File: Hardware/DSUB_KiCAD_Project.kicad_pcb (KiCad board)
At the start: 4 copper layers, 112.2 x 87.2 mm, 6 parts, among them J1 DB37_Female, J11 DB37_Female, J3 DB37_Female, J5 DB37_Female, J7 DB37_Female, J9 DB37_Female

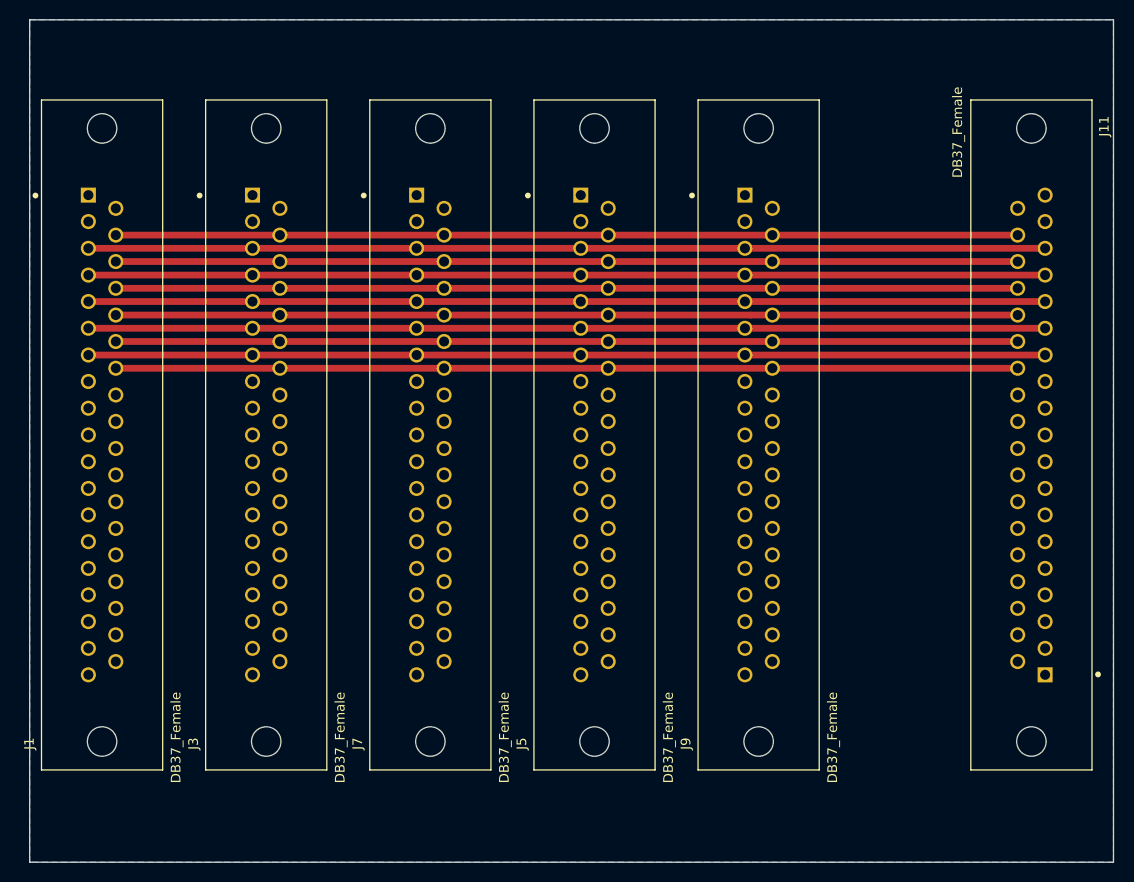
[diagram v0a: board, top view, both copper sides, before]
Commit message: rounded corners
corners were rounded to 5mm
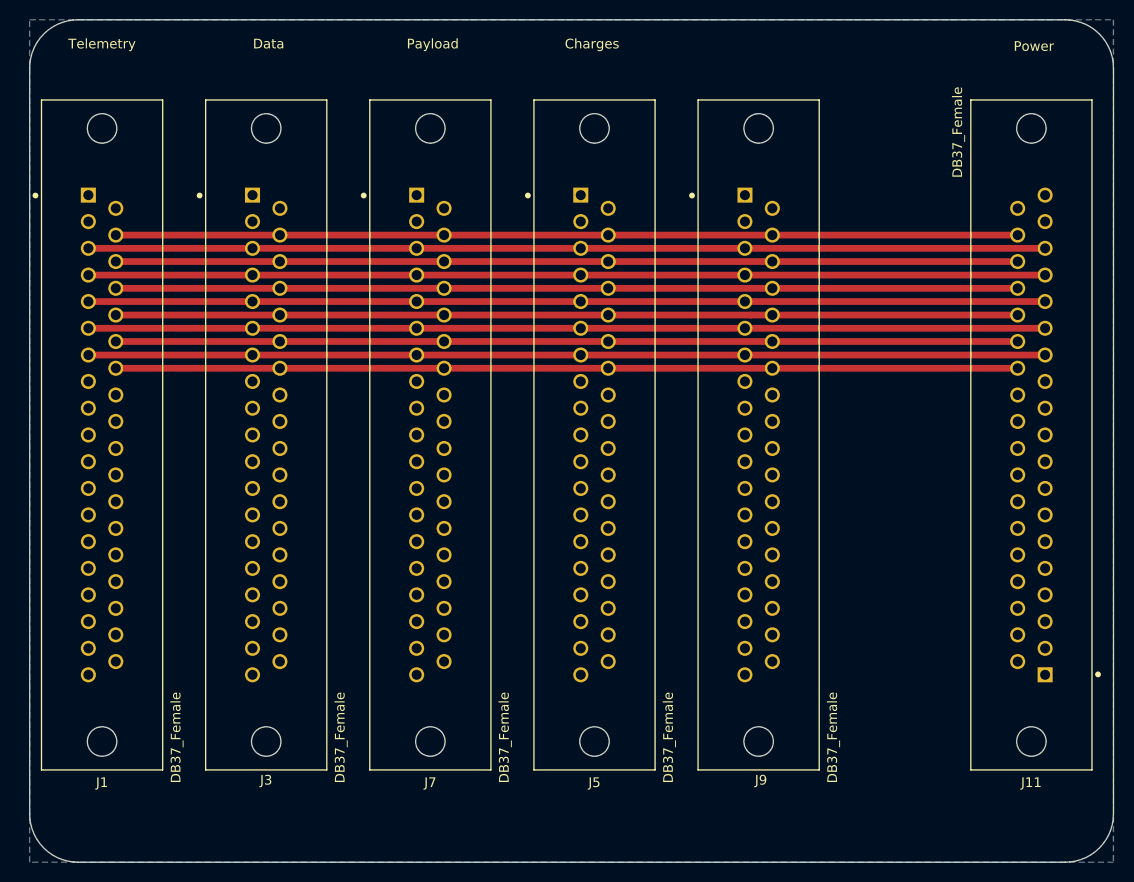
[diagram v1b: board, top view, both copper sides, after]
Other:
- outline, holes or cut-outs redrawn
- board text added: "Data"
- board text removed: "data"
